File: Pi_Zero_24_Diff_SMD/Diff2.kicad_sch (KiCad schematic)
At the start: 14 parts, among them J7 Diff Out, J8 Diff Out, U7 AM26C31, U8 AM26C31

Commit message: generated WIP PCB
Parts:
- C8, C9: footprint (none) -> Capacitor_SMD:C_0603_1608Metric_Pad1.08x0.95mm_HandSolder
- J7, J8: footprint (none) -> Scotts:RJ45_Amphenol_54602-x08_Horizontal
- R14, R15, R16, R17, R18, R19, R20, R21: footprint (none) -> Resistor_SMD:R_0603_1608Metric_Pad0.98x0.95mm_HandSolder
- U7, U8: footprint (none) -> Package_SO:SOIC-16_3.9x9.9mm_P1.27mm
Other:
- title: Pi_Zero_24_Diff -> Pi Zero 24 Diff
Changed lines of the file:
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@@
   (paper "A4")
   (title_block
-    (title "Pi_Zero_24_Diff")
-    (date "2022-08-20")
+    (title "Pi Zero 24 Diff")
+    (date "2022-08-31")
     (rev "v1")
     (company "Scott Hanson")
@@
       (effects (font (size 1.27 1.27)) (justify left))
     )
-    (property "Footprint" "" (id 2) (at 124.714 50.927 90)
+    (property "Footprint" "Resistor_SMD:R_0603_1608Metric_Pad0.98x0.95mm_HandSolder" (id 2) (at 124.714 50.927 90)
       (effects (font (size 1.27 1.27)) hide)
     )
@@
       (effects (font (size 1.27 1.27)) (justify left))
     )
-    (property "Footprint" "" (id 2) (at 189.1792 44.704 0)
+    (property "Footprint" "Capacitor_SMD:C_0603_1608Metric_Pad1.08x0.95mm_HandSolder" (id 2) (at 189.1792 44.704 0)
       (effects (font (size 1.27 1.27)) hide)
     )
@@
       (effects (font (size 1.27 1.27)) (justify left))
     )
-    (property "Footprint" "" (id 2) (at 120.904 101.981 90)
+    (property "Footprint" "Resistor_SMD:R_0603_1608Metric_Pad0.98x0.95mm_HandSolder" (id 2) (at 120.904 101.981 90)
       (effects (font (size 1.27 1.27)) hide)
     )
@@
       (effects (font (size 1.27 1.27)) (justify left))
     )
-    (property "Footprint" "" (id 2) (at 124.714 35.306 90)
+    (property "Footprint" "Resistor_SMD:R_0603_1608Metric_Pad0.98x0.95mm_HandSolder" (id 2) (at 124.714 35.306 90)
       (effects (font (size 1.27 1.27)) hide)
     )
@@
     (property "Reference" "U8" (id 0) (at 170.434 35.814 0))
     (property "Value" "AM26C31" (id 1) (at 170.434 38.1254 0))
-    (property "Footprint" "" (id 2) (at 175.514 77.089 0)
+    (property "Footprint" "Package_SO:SOIC-16_3.9x9.9mm_P1.27mm" (id 2) (at 175.514 77.089 0)
       (effects (font (size 1.27 1.27)) (justify left) hide)
     )
@@
       (effects (font (size 1.27 1.27)) (justify left))
     )
-    (property "Footprint" "" (id 2) (at 185.3692 105.029 0)
+    (property "Footprint" "Capacitor_SMD:C_0603_1608Metric_Pad1.08x0.95mm_HandSolder" (id 2) (at 185.3692 105.029 0)
       (effects (font (size 1.27 1.27)) hide)
     )
@@
       (effects (font (size 1.27 1.27)) (justify left))
     )
-    (property "Footprint" "" (id 2) (at 120.904 111.887 90)
+    (property "Footprint" "Resistor_SMD:R_0603_1608Metric_Pad0.98x0.95mm_HandSolder" (id 2) (at 120.904 111.887 90)
       (effects (font (size 1.27 1.27)) hide)
     )
@@
       (effects (font (size 1.27 1.27)) (justify left))
     )
-    (property "Footprint" "" (id 2) (at 124.714 33.782 90)
+    (property "Footprint" "Resistor_SMD:R_0603_1608Metric_Pad0.98x0.95mm_HandSolder" (id 2) (at 124.714 33.782 90)
       (effects (font (size 1.27 1.27)) hide)
     )
@@
     (property "Reference" "J7" (id 0) (at 109.6518 145.4658 0))
     (property "Value" "Diff Out" (id 1) (at 109.6518 143.1544 0))
-    (property "Footprint" "" (id 2) (at 108.204 129.159 90)
+    (property "Footprint" "Scotts:RJ45_Amphenol_54602-x08_Horizontal" (id 2) (at 108.204 129.159 90)
       (effects (font (size 1.27 1.27)) hide)
     )
@@
     (property "Reference" "U7" (id 0) (at 167.259 96.774 0))
     (property "Value" "AM26C31" (id 1) (at 167.259 99.0854 0))
-    (property "Footprint" "" (id 2) (at 172.339 138.049 0)
+    (property "Footprint" "Package_SO:SOIC-16_3.9x9.9mm_P1.27mm" (id 2) (at 172.339 138.049 0)
       (effects (font (size 1.27 1.27)) (justify left) hide)
     )
@@
       (effects (font (size 1.27 1.27)) (justify left))
     )
-    (property "Footprint" "" (id 2) (at 120.904 96.266 90)
+    (property "Footprint" "Resistor_SMD:R_0603_1608Metric_Pad0.98x0.95mm_HandSolder" (id 2) (at 120.904 96.266 90)
       (effects (font (size 1.27 1.27)) hide)
     )
@@
       (effects (font (size 1.27 1.27)) (justify left))
     )
-    (property "Footprint" "" (id 2) (at 124.079 41.021 90)
+    (property "Footprint" "Resistor_SMD:R_0603_1608Metric_Pad0.98x0.95mm_HandSolder" (id 2) (at 124.079 41.021 90)
       (effects (font (size 1.27 1.27)) hide)
     )
@@
       (effects (font (size 1.27 1.27)) (justify left))
     )
-    (property "Footprint" "" (id 2) (at 120.904 94.742 90)
+    (property "Footprint" "Resistor_SMD:R_0603_1608Metric_Pad0.98x0.95mm_HandSolder" (id 2) (at 120.904 94.742 90)
       (effects (font (size 1.27 1.27)) hide)
     )
@@
     (property "Reference" "J8" (id 0) (at 107.569 52.959 0))
     (property "Value" "Diff Out" (id 1) (at 108.839 54.864 0))
-    (property "Footprint" "" (id 2) (at 108.839 67.564 90)
-      (effects (font (size 1.27 1.27)) hide)
-    )
+    (property "Footprint" "Scotts:RJ45_Amphenol_54602-x08_Horizontal" (id 2) (at 108.839 67.564 90)
+      (effects (font (size 1.27 1.27)) hide)
+    )

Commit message: working on routing
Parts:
- J5: renamed from J7; value Diff Out -> Diff Out 3
- J6: renamed from J8; value Diff Out -> Diff Out 4
- renumbered C8 to C6, C9 to C7, U7 to U5, U8 to U6
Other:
- moved on the sheet: C6, C7, J5, J6, R14, R15, R16, R17, R18, R19, R20, R21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

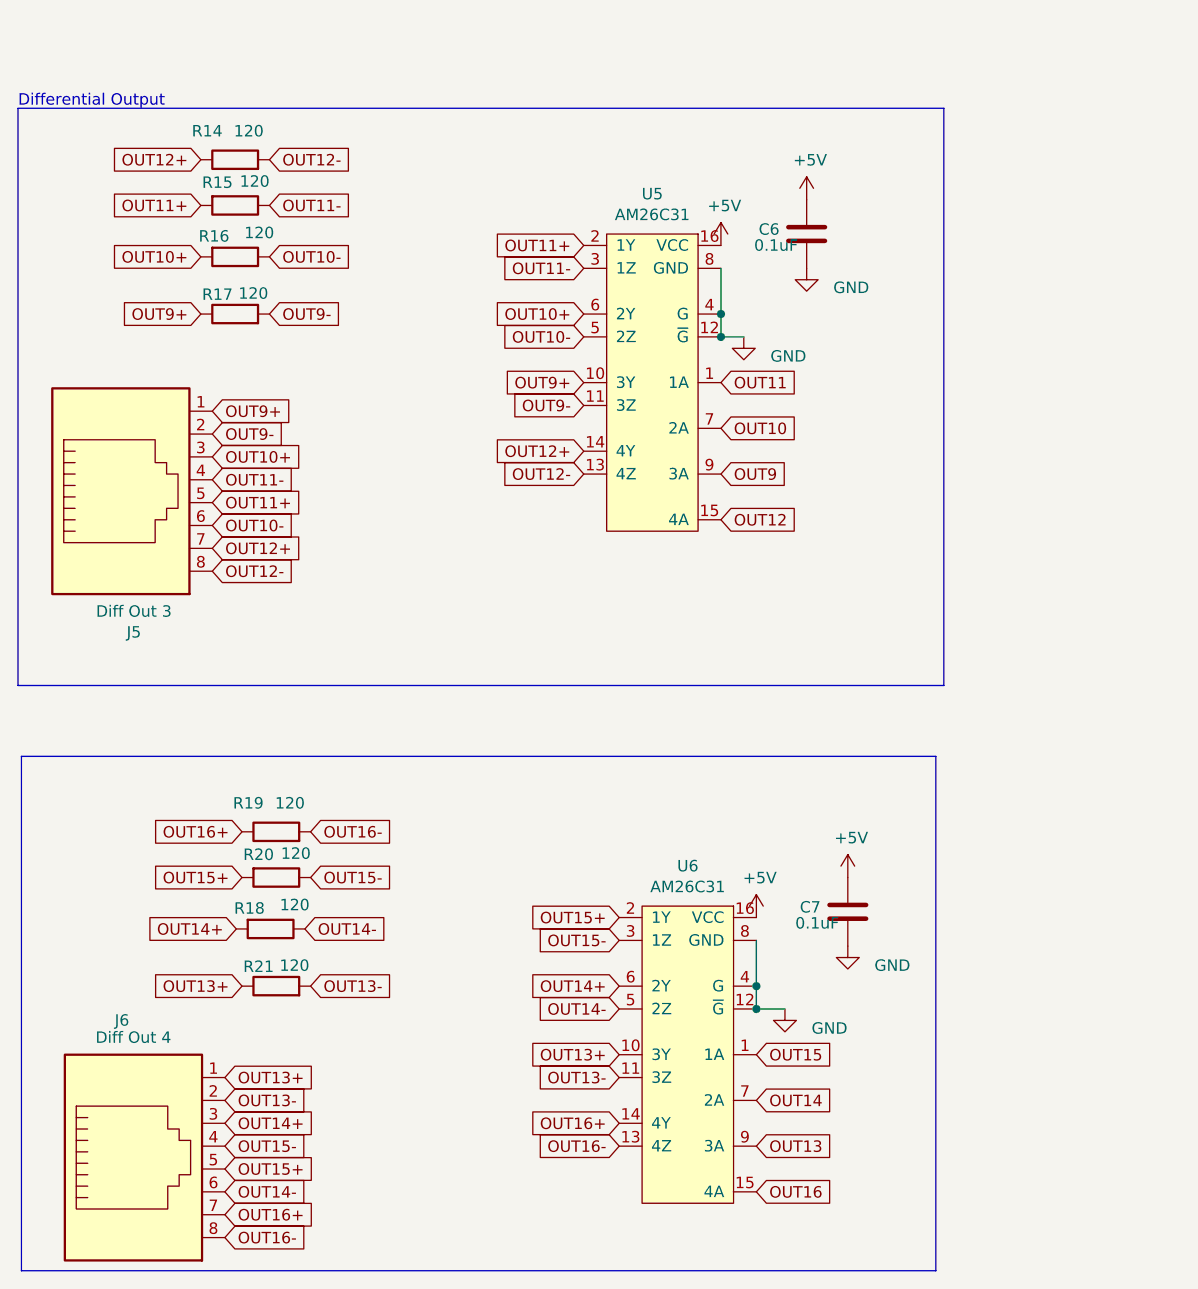
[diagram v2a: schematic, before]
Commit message: added PI Zero Diff
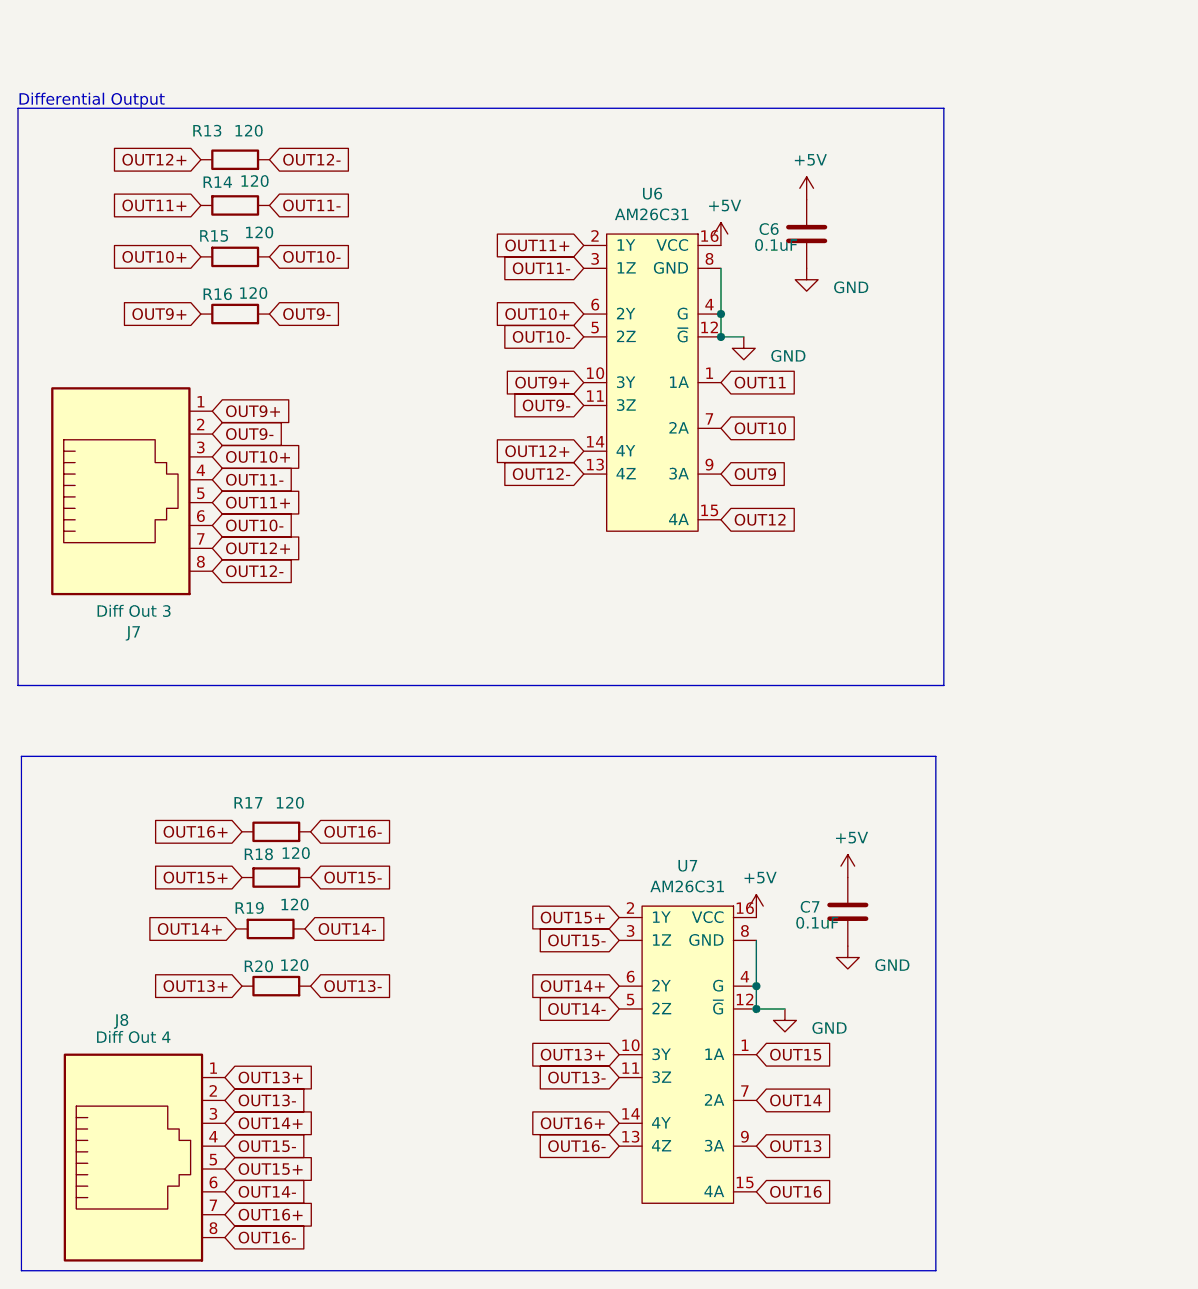
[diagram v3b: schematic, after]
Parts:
- J7: renamed from J5; LCSC C2938579 -> C86492
- J8: renamed from J6; LCSC C2938579 -> C86492
- renumbered R14 to R13, R15 to R14, R16 to R15, R17 to R16, R19 to R17, R20 to R18, R18 to R19, R21 to R20, U5 to U6, U6 to U7
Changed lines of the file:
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@@
   (symbol (lib_id "Device:R") (at 99.187 131.191 90) (unit 1)
     (in_bom yes) (on_board yes)
-    (property "Reference" "R21" (id 0) (at 98.933 129.032 90)
+    (property "Reference" "R20" (id 0) (at 98.933 129.032 90)
       (effects (font (size 1.27 1.27)) (justify left))
     )
@@
   (symbol (lib_id "power:GND") (at 158.115 51.435 0) (unit 1)
     (in_bom yes) (on_board yes)
-    (property "Reference" "#PWR045" (id 0) (at 158.115 57.785 0)
+    (property "Reference" "#PWR035" (id 0) (at 158.115 57.785 0)
       (effects (font (size 1.27 1.27)) hide)
     )
@@
   (symbol (lib_id "power:+5V") (at 148.59 48.895 0) (unit 1)
     (in_bom yes) (on_board yes)
-    (property "Reference" "#PWR040" (id 0) (at 148.59 52.705 0)
+    (property "Reference" "#PWR034" (id 0) (at 148.59 52.705 0)
       (effects (font (size 1.27 1.27)) hide)
     )
@@
   (symbol (lib_id "Device:R") (at 94.615 50.165 270) (unit 1)
     (in_bom yes) (on_board yes)
-    (property "Reference" "R16" (id 0) (at 90.551 47.879 90)
+    (property "Reference" "R15" (id 0) (at 90.551 47.879 90)
       (effects (font (size 1.27 1.27)) (justify left))
     )
@@
   (symbol (lib_id "power:GND") (at 162.687 126.746 0) (unit 1)
     (in_bom yes) (on_board yes)
-    (property "Reference" "#PWR047" (id 0) (at 162.687 133.096 0)
+    (property "Reference" "#PWR039" (id 0) (at 162.687 133.096 0)
       (effects (font (size 1.27 1.27)) hide)
     )
@@
   (symbol (lib_id "Device:R") (at 99.187 119.126 270) (unit 1)
     (in_bom yes) (on_board yes)
-    (property "Reference" "R20" (id 0) (at 95.504 116.586 90)
+    (property "Reference" "R18" (id 0) (at 95.504 116.586 90)
       (effects (font (size 1.27 1.27)) (justify left))
     )
@@
   (symbol (lib_id "AM26C31:AM26C31") (at 144.907 138.811 0) (mirror y) (unit 1)
     (in_bom yes) (on_board yes)
-    (property "Reference" "U6" (id 0) (at 144.907 117.856 0))
+    (property "Reference" "U7" (id 0) (at 144.907 117.856 0))
     (property "Value" "AM26C31" (id 1) (at 144.907 120.1674 0))
     (property "Footprint" "Package_SO:SOIC-16_3.9x9.9mm_P1.27mm" (id 2) (at 149.987 159.131 0)
@@
   (symbol (lib_id "power:GND") (at 151.13 59.055 0) (unit 1)
     (in_bom yes) (on_board yes)
-    (property "Reference" "#PWR041" (id 0) (at 151.13 65.405 0)
+    (property "Reference" "#PWR036" (id 0) (at 151.13 65.405 0)
       (effects (font (size 1.27 1.27)) hide)
     )
@@
   (symbol (lib_id "power:+5V") (at 162.687 119.126 0) (unit 1)
     (in_bom yes) (on_board yes)
-    (property "Reference" "#PWR046" (id 0) (at 162.687 122.936 0)
+    (property "Reference" "#PWR037" (id 0) (at 162.687 122.936 0)
       (effects (font (size 1.27 1.27)) hide)
     )
@@
   (symbol (lib_id "Device:R") (at 94.615 56.515 90) (unit 1)
     (in_bom yes) (on_board yes)
-    (property "Reference" "R17" (id 0) (at 94.361 54.356 90)
+    (property "Reference" "R16" (id 0) (at 94.361 54.356 90)
       (effects (font (size 1.27 1.27)) (justify left))
     )
@@
   (symbol (lib_id "power:+5V") (at 158.115 43.815 0) (unit 1)
     (in_bom yes) (on_board yes)
-    (property "Reference" "#PWR044" (id 0) (at 158.115 47.625 0)
+    (property "Reference" "#PWR033" (id 0) (at 158.115 47.625 0)
       (effects (font (size 1.27 1.27)) hide)
     )
@@
   (symbol (lib_id "power:+5V") (at 152.527 123.571 0) (unit 1)
     (in_bom yes) (on_board yes)
-    (property "Reference" "#PWR042" (id 0) (at 152.527 127.381 0)
+    (property "Reference" "#PWR038" (id 0) (at 152.527 127.381 0)
       (effects (font (size 1.27 1.27)) hide)
     )
@@
   (symbol (lib_id "Device:R") (at 99.187 114.046 90) (unit 1)
     (in_bom yes) (on_board yes)
-    (property "Reference" "R19" (id 0) (at 97.79 110.871 90)
+    (property "Reference" "R17" (id 0) (at 97.79 110.871 90)
       (effects (font (size 1.27 1.27)) (justify left))
     )
@@
   (symbol (lib_id "power:GND") (at 155.702 133.731 0) (unit 1)
     (in_bom yes) (on_board yes)
-    (property "Reference" "#PWR043" (id 0) (at 155.702 140.081 0)
+    (property "Reference" "#PWR040" (id 0) (at 155.702 140.081 0)
       (effects (font (size 1.27 1.27)) hide)
     )
@@
   (symbol (lib_id "Connector:RJ45") (at 81.915 74.93 0) (mirror x) (unit 1)
     (in_bom yes) (on_board yes)
-    (property "Reference" "J5" (id 0) (at 83.3628 91.8718 0))
+    (property "Reference" "J7" (id 0) (at 83.3628 91.8718 0))
     (property "Value" "Diff Out 3" (id 1) (at 83.3628 89.5604 0))
     (property "Footprint" "Scotts:RJ45_Amphenol_54602-x08_Horizontal" (id 2) (at 81.915 75.565 90)
@@
       (effects (font (size 1.27 1.27)) hide)
     )
-    (property "LCSC" "C2938579" (id 6) (at 83.3628 91.8718 0)
+    (property "LCSC" "C86492" (id 6) (at 83.3628 91.8718 0)
       (effects (font (size 1.27 1.27)) hide)
     )
@@
   (symbol (lib_id "AM26C31:AM26C31") (at 140.97 64.135 0) (mirror y) (unit 1)
     (in_bom yes) (on_board yes)
-    (property "Reference" "U5" (id 0) (at 140.97 43.18 0))
+    (property "Reference" "U6" (id 0) (at 140.97 43.18 0))
     (property "Value" "AM26C31" (id 1) (at 140.97 45.4914 0))
     (property "Footprint" "Package_SO:SOIC-16_3.9x9.9mm_P1.27mm" (id 2) (at 146.05 84.455 0)
@@
   (symbol (lib_id "Device:R") (at 94.615 44.45 270) (unit 1)
     (in_bom yes) (on_board yes)
-    (property "Reference" "R15" (id 0) (at 90.932 41.91 90)
+    (property "Reference" "R14" (id 0) (at 90.932 41.91 90)
       (effects (font (size 1.27 1.27)) (justify left))
     )
@@
   (symbol (lib_id "Device:R") (at 98.552 124.841 270) (unit 1)
     (in_bom yes) (on_board yes)
-    (property "Reference" "R18" (id 0) (at 94.488 122.555 90)
+    (property "Reference" "R19" (id 0) (at 94.488 122.555 90)
       (effects (font (size 1.27 1.27)) (justify left))
     )
@@
   (symbol (lib_id "Device:R") (at 94.615 39.37 90) (unit 1)
     (in_bom yes) (on_board yes)
-    (property "Reference" "R14" (id 0) (at 93.218 36.195 90)
+    (property "Reference" "R13" (id 0) (at 93.218 36.195 90)
       (effects (font (size 1.27 1.27)) (justify left))
     )
@@
   (symbol (lib_id "Connector:RJ45") (at 83.312 148.971 0) (mirror x) (unit 1)
     (in_bom yes) (on_board yes)
-    (property "Reference" "J6" (id 0) (at 82.042 135.001 0))
+    (property "Reference" "J8" (id 0) (at 82.042 135.001 0))
     (property "Value" "Diff Out 4" (id 1) (at 83.312 136.906 0))
     (property "Footprint" "Scotts:RJ45_Amphenol_54602-x08_Horizontal" (id 2) (at 83.312 149.606 90)
@@
       (effects (font (size 1.27 1.27)) hide)
     )
-    (property "LCSC" "C2938579" (id 6) (at 82.042 135.001 0)
-      (effects (font (size 1.27 1.27)) hide)
-    )
+    (property "LCSC" "C86492" (id 6) (at 82.042 135.001 0)
+      (effects (font (size 1.27 1.27)) hide)
+    )
